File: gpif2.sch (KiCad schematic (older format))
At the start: 38 parts, among them Q3 IRLML2502, SW1 SW_IL, U1 xc7a50tftg256

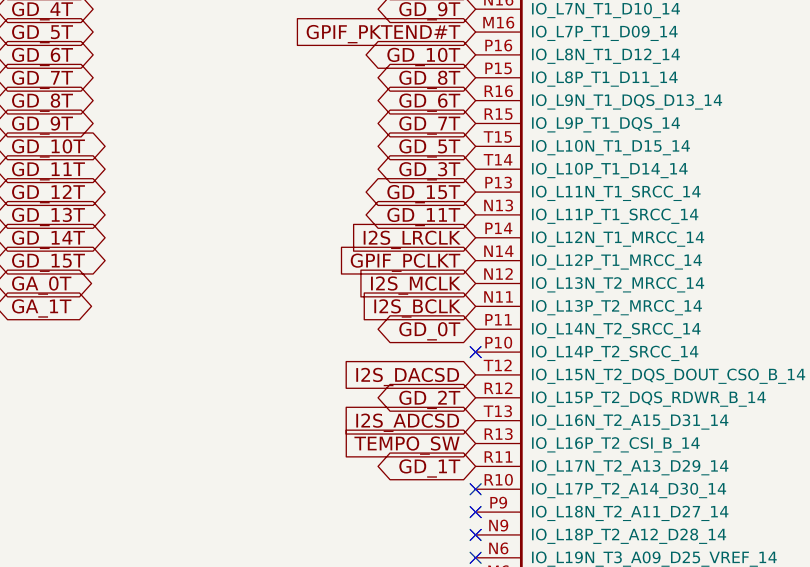
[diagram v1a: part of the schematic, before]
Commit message: finished most non-priority connections and placed power/gnd planes
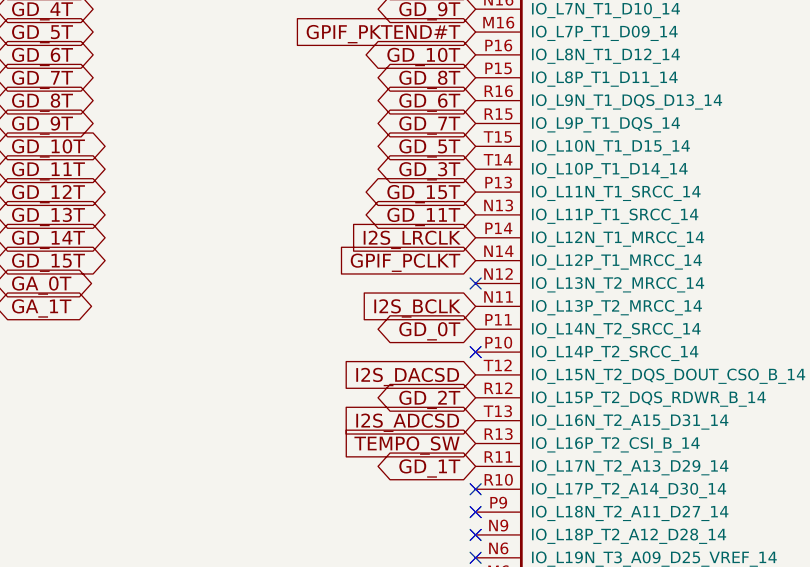
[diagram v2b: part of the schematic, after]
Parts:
- R33: footprint Resistors_SMD:R_1206 -> Resistors_SMD:R_0402
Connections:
- net I2S_MCLK: no longer names the net of U1.N12 (IO_L13N_T2_MRCC_14)
- no-connect marks 17 -> 18
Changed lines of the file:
@@
 LIBS:au-y1008-2
 LIBS:hdmi_conn
+LIBS:wayne_and_layne_kicad_symbols
 EELAYER 25 0
 EELAYER END
@@
 Text GLabel 5950 3950 0    60   Input ~ 0
 I2S_LRCLK
-Text GLabel 5950 4150 0    60   Input ~ 0
-I2S_MCLK
 Text GLabel 5950 4250 0    60   Input ~ 0
 I2S_BCLK
@@
 F 0 "R33" H 10030 3670 50  0000 L CNN
 F 1 "165" H 10030 3610 50  0000 L CNN
-F 2 "Resistors_SMD:R_1206" H 10000 3650 50  0001 C CNN
+F 2 "Resistors_SMD:R_0402" H 10000 3650 50  0001 C CNN
 F 3 "" H 10000 3650 50  0000 C CNN
 	1    10000 3650
@@
 GD_1T
 NoConn ~ 5950 1550
+NoConn ~ 5950 4150
 $EndSCHEMATC

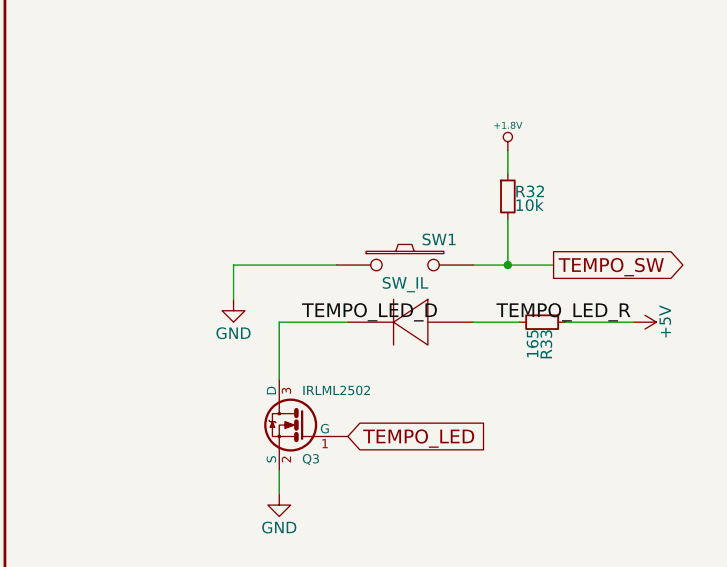
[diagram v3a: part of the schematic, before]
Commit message: changed led driver footprint, added the appropriate amount of clearence for audio jacks, redid all those connections, etc, etc
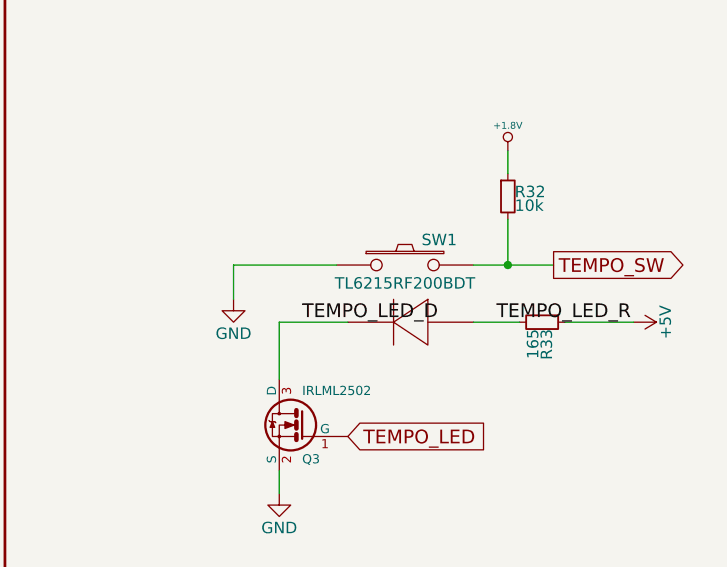
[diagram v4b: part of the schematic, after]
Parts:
- SW1: value SW_IL -> TL6215RF200BDT
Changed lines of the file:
@@
 LIBS:wayne_and_layne_kicad_symbols
 LIBS:m24m02-dr
+LIBS:fxo-hc73
 EELAYER 25 0
 EELAYER END
@@
 P 9400 3400
 F 0 "SW1" H 9550 3510 50  0000 C CNN
-F 1 "SW_IL" H 9400 3320 50  0000 C CNN
+F 1 "TL6215RF200BDT" H 9400 3320 50  0000 C CNN
 F 2 "DFTcustom:tl6215_right_angle" H 9400 3400 50  0001 C CNN
 F 3 "" H 9400 3400 50  0000 C CNN

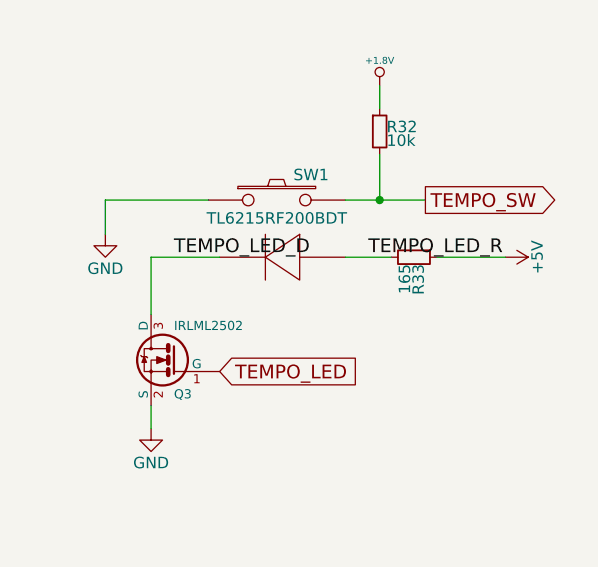
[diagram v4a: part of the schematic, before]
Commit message: completed BOM, changed footprints and values of identical components (ex. 100nf -> .1uF), have yet to update PCBNEW to reflect footprint changes
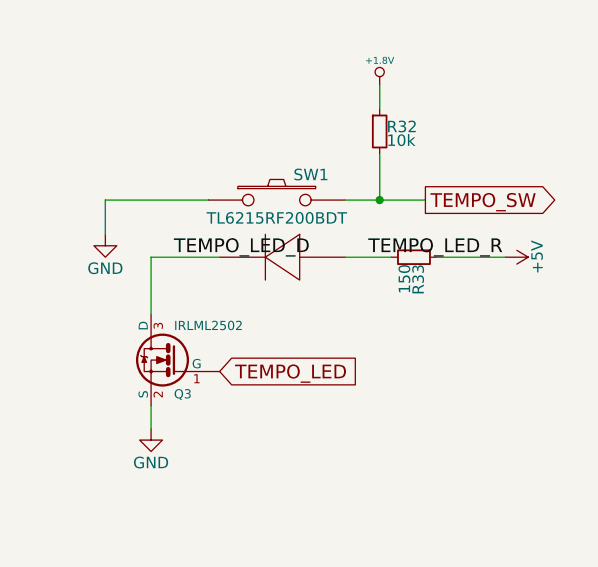
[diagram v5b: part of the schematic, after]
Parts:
- R33: value 165 -> 150
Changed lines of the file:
@@
 P 10000 3650
 F 0 "R33" H 10030 3670 50  0000 L CNN
-F 1 "165" H 10030 3610 50  0000 L CNN
+F 1 "150" H 10030 3610 50  0000 L CNN
 F 2 "Resistors_SMD:R_0402" H 10000 3650 50  0001 C CNN
 F 3 "" H 10000 3650 50  0000 C CNN

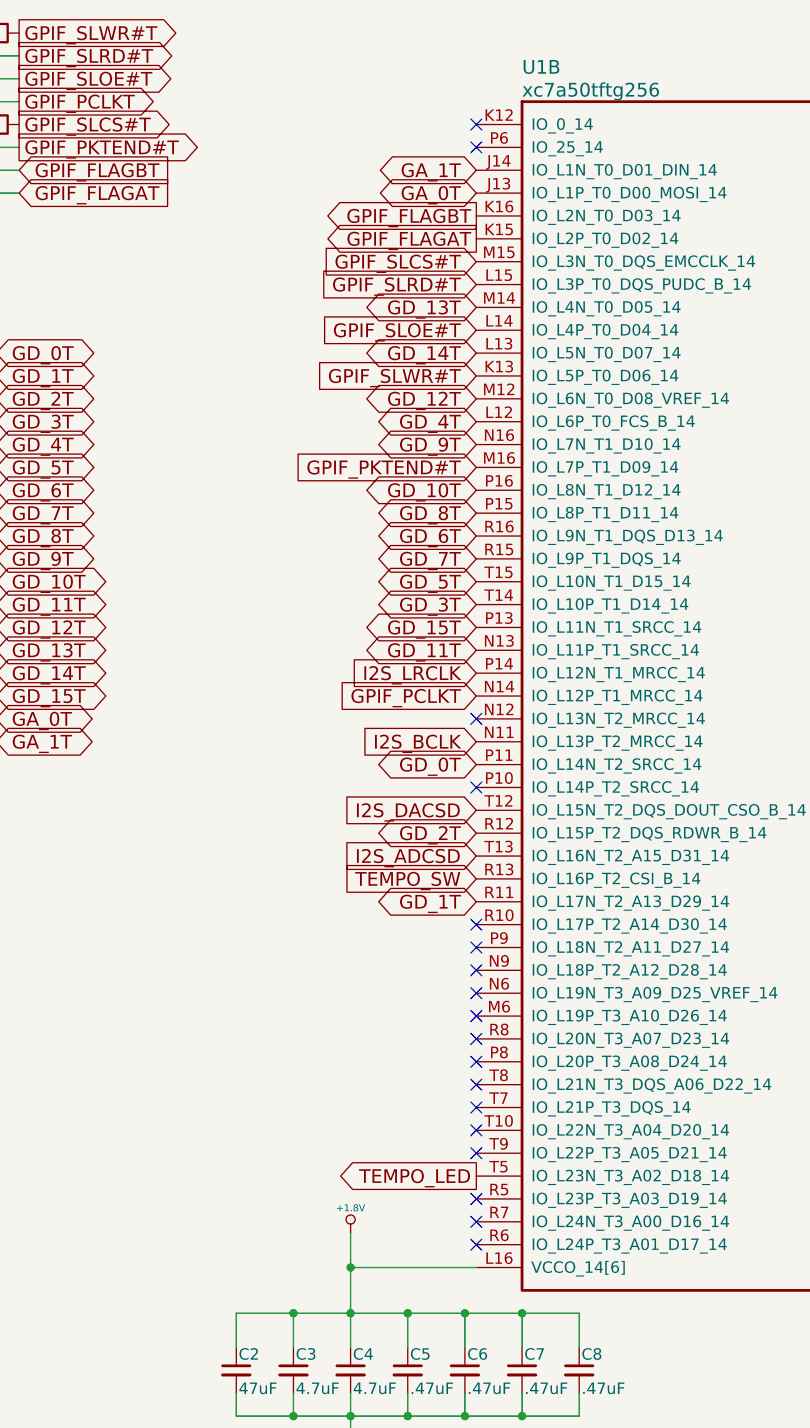
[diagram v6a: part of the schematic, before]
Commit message: added configuration data line, other small changes
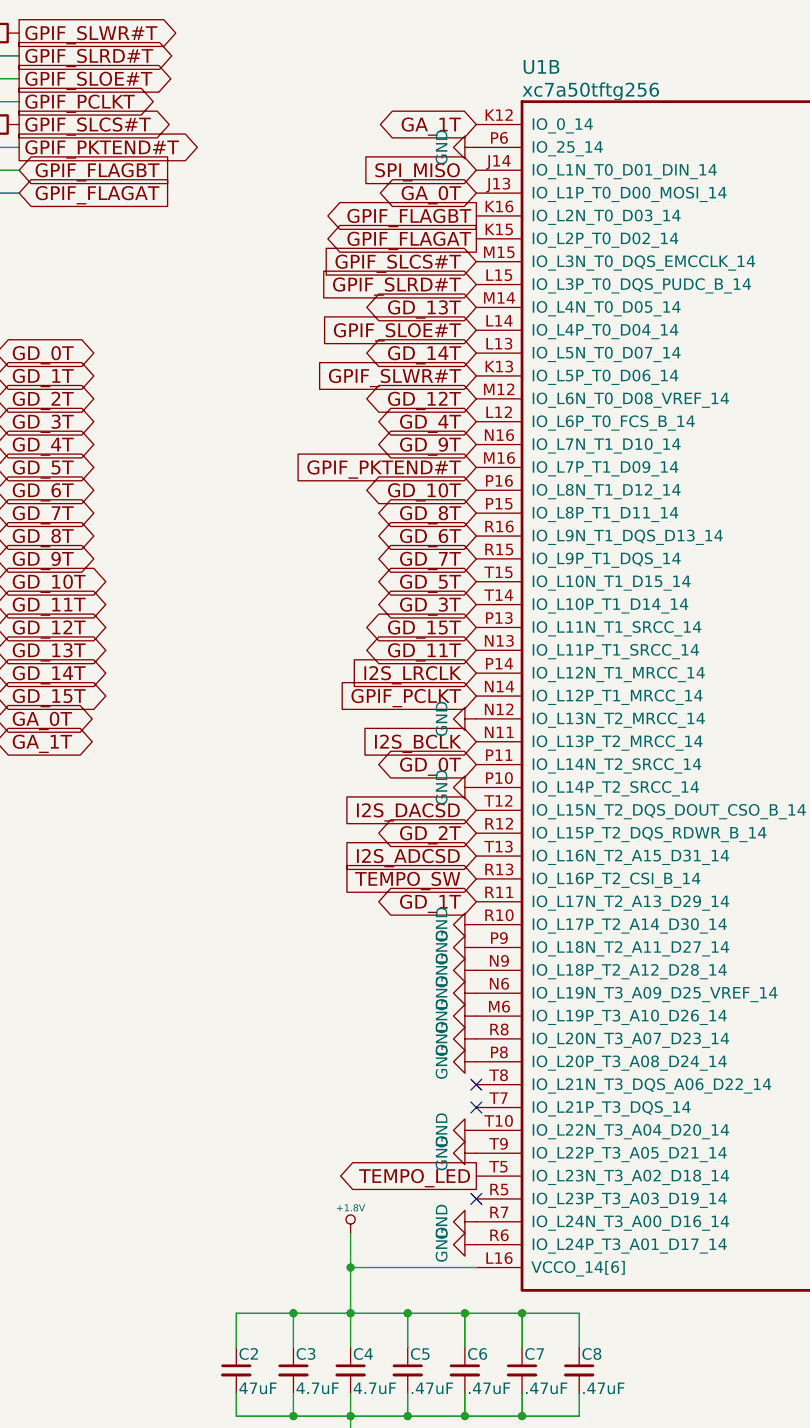
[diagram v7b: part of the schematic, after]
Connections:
- net GA_1T: now also U1.K12 (IO_0_14); no longer U1.J14 (IO_L1N_T0_D01_DIN_14)
- net GND: now also U1.M6 (IO_L19P_T3_A10_D26_14), U1.N12 (IO_L13N_T2_MRCC_14), U1.N6 (IO_L19N_T3_A09_D25_VREF_14), U1.N9 (IO_L18P_T2_A12_D28_14), U1.P10 (IO_L14P_T2_SRCC_14), U1.P6 (IO_25_14), U1.P8 (IO_L20P_T3_A08_D24_14), U1.P9 (IO_L18N_T2_A11_D27_14), U1.R10 (IO_L17P_T2_A14_D30_14), U1.R6 (IO_L24P_T3_A01_D17_14), U1.R7 (IO_L24N_T3_A00_D16_14), U1.R8 (IO_L20N_T3_A07_D23_14), U1.T10 (IO_L22N_T3_A04_D20_14), U1.T9 (IO_L22P_T3_A05_D21_14)
- new net SPI_MISO: U1.J14 (IO_L1N_T0_D01_DIN_14)
- no-connect marks 18 -> 3
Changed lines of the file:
@@
 $EndComp
 $Comp
-L +1.8V #PWR12
+L +1.8V #PWR012
 U 1 1 585C5E93
 P 5400 6400
-F 0 "#PWR12" H 5400 6540 20  0001 C CNN
+F 0 "#PWR012" H 5400 6540 20  0001 C CNN
 F 1 "+1.8V" H 5400 6510 30  0000 C CNN
 F 2 "" H 5400 6400 60  0001 C CNN
@@
 Text GLabel 2700 1450 0    60   Input ~ 0
 GPIF_PCLK
-NoConn ~ 5950 5550
 NoConn ~ 5950 6250
-NoConn ~ 5950 5050
-NoConn ~ 5950 5150
-NoConn ~ 5950 5250
-NoConn ~ 5950 5350
-NoConn ~ 5950 5450
-NoConn ~ 5950 6350
-NoConn ~ 5950 6450
 $Comp
 L C_Small C2
@@
 Connection ~ 5150 7200
 $Comp
-L GND #PWR13
+L GND #PWR013
 U 1 1 586C88E4
 P 5400 7300
-F 0 "#PWR13" H 5400 7050 50  0001 C CNN
+F 0 "#PWR013" H 5400 7050 50  0001 C CNN
 F 1 "GND" H 5400 7150 50  0000 C CNN
 F 2 "" H 5400 7300 50  0000 C CNN
@@
 Text GLabel 5950 4250 0    60   Input ~ 0
 I2S_BCLK
-NoConn ~ 5950 4450
 Text GLabel 5950 4550 0    60   Input ~ 0
 I2S_DACSD
@@
 $EndComp
 $Comp
-L GND #PWR14
+L GND #PWR014
 U 1 1 587AD7CC
 P 8650 3550
-F 0 "#PWR14" H 8650 3300 50  0001 C CNN
+F 0 "#PWR014" H 8650 3300 50  0001 C CNN
 F 1 "GND" H 8650 3400 50  0000 C CNN
 F 2 "" H 8650 3550 50  0000 C CNN
@@
 $EndComp
 $Comp
-L GND #PWR15
+L GND #PWR015
 U 1 1 587B04F2
 P 8850 4400
-F 0 "#PWR15" H 8850 4150 50  0001 C CNN
+F 0 "#PWR015" H 8850 4150 50  0001 C CNN
 F 1 "GND" H 8850 4250 50  0000 C CNN
 F 2 "" H 8850 4400 50  0000 C CNN
@@
 	9700 3650 9900 3650
 $Comp
-L +5V #PWR17
+L +5V #PWR016
 U 1 1 587B1756
 P 10400 3650
-F 0 "#PWR17" H 10400 3500 50  0001 C CNN
+F 0 "#PWR016" H 10400 3500 50  0001 C CNN
 F 1 "+5V" H 10400 3790 50  0000 C CNN
 F 2 "" H 10400 3650 50  0000 C CNN
@@
 Text GLabel 5950 4750 0    60   Input ~ 0
 I2S_ADCSD
-NoConn ~ 5950 5650
 $Comp
 L R R30
@@
 	9700 3400 10050 3400
 $Comp
-L +1.8V #PWR16
+L +1.8V #PWR017
 U 1 1 588410AE
 P 9850 2900
-F 0 "#PWR16" H 9850 3040 20  0001 C CNN
+F 0 "#PWR017" H 9850 3040 20  0001 C CNN
 F 1 "+1.8V" H 9850 3010 30  0000 C CNN
 F 2 "" H 9850 2900 60  0001 C CNN
@@
 Text Label 8950 3650 0    60   ~ 0
 TEMPO_LED_D
-NoConn ~ 5950 1650
 NoConn ~ 5950 5850
 NoConn ~ 5950 5750
-NoConn ~ 5950 5950
-NoConn ~ 5950 6050
 Text GLabel 5950 2250 0    60   Input ~ 0
 GPIF_SLRD#T
@@
 Text GLabel 5950 4050 0    60   Input ~ 0
 GPIF_PCLKT
-Text GLabel 5950 1750 0    60   BiDi ~ 0
+Text GLabel 5950 1550 0    60   BiDi ~ 0
 GA_1T
 Text GLabel 5950 1850 0    60   BiDi ~ 0
@@
 Text GLabel 5950 4950 0    60   BiDi ~ 0
 GD_1T
-NoConn ~ 5950 1550
-NoConn ~ 5950 4150
+$Comp
+L GND #PWR018
+U 1 1 58945BF9
+P 5950 4150
+F 0 "#PWR018" H 5950 3900 50  0001 C CNN
+F 1 "GND" H 5950 4000 50  0000 C CNN
+F 2 "" H 5950 4150 50  0000 C CNN
+F 3 "" H 5950 4150 50  0000 C CNN
+	1    5950 4150
+	0    1    1    0
+$EndComp
+$Comp
+L GND #PWR019
+U 1 1 589461C0
+P 5950 4450
+F 0 "#PWR019" H 5950 4200 50  0001 C CNN
+F 1 "GND" H 5950 4300 50  0000 C CNN
+F 2 "" H 5950 4450 50  0000 C CNN
+F 3 "" H 5950 4450 50  0000 C CNN
+	1    5950 4450
+	0    1    1    0
+$EndComp
+$Comp
+L GND #PWR020
+U 1 1 58946355
+P 5950 5050
+F 0 "#PWR020" H 5950 4800 50  0001 C CNN
+F 1 "GND" H 5950 4900 50  0000 C CNN
+F 2 "" H 5950 5050 50  0000 C CNN
+F 3 "" H 5950 5050 50  0000 C CNN
+	1    5950 5050
+	0    1    1    0
+$EndComp
+$Comp
+L GND #PWR021
+U 1 1 58946634
+P 5950 5950
+F 0 "#PWR021" H 5950 5700 50  0001 C CNN
+F 1 "GND" H 5950 5800 50  0000 C CNN
+F 2 "" H 5950 5950 50  0000 C CNN
+F 3 "" H 5950 5950 50  0000 C CNN
+	1    5950 5950
+	0    1    1    0
+$EndComp
+$Comp
+L GND #PWR022
+U 1 1 589483E2
+P 5950 1650
+F 0 "#PWR022" H 5950 1400 50  0001 C CNN
+F 1 "GND" H 5950 1500 50  0000 C CNN
+F 2 "" H 5950 1650 50  0000 C CNN
+F 3 "" H 5950 1650 50  0000 C CNN
+	1    5950 1650
+	0    1    1    0
+$EndComp
+$Comp
+L GND #PWR023
+U 1 1 58948C63
+P 5950 6450
+F 0 "#PWR023" H 5950 6200 50  0001 C CNN
+F 1 "GND" H 5950 6300 50  0000 C CNN
+F 2 "" H 5950 6450 50  0000 C CNN
+F 3 "" H 5950 6450 50  0000 C CNN
+	1    5950 6450
+	0    1    1    0
+$EndComp
+$Comp
+L GND #PWR024
+U 1 1 5894C026
+P 5950 6350
+F 0 "#PWR024" H 5950 6100 50  0001 C CNN
+F 1 "GND" H 5950 6200 50  0000 C CNN
+F 2 "" H 5950 6350 50  0000 C CNN
+F 3 "" H 5950 6350 50  0000 C CNN
+	1    5950 6350
+	0    1    1    0
+$EndComp
+$Comp
+L GND #PWR025
+U 1 1 5894C0A3
+P 5950 5650
+F 0 "#PWR025" H 5950 5400 50  0001 C CNN
+F 1 "GND" H 5950 5500 50  0000 C CNN
+F 2 "" H 5950 5650 50  0000 C CNN
+F 3 "" H 5950 5650 50  0000 C CNN
+	1    5950 5650
+	0    1    1    0
+$EndComp
+$Comp
+L GND #PWR026
+U 1 1 5894C120
+P 5950 5550
+F 0 "#PWR026" H 5950 5300 50  0001 C CNN
+F 1 "GND" H 5950 5400 50  0000 C CNN
+F 2 "" H 5950 5550 50  0000 C CNN
+F 3 "" H 5950 5550 50  0000 C CNN
+	1    5950 5550
+	0    1    1    0
+$EndComp
+$Comp
+L GND #PWR027
+U 1 1 5894C19D
+P 5950 5250
+F 0 "#PWR027" H 5950 5000 50  0001 C CNN
+F 1 "GND" H 5950 5100 50  0000 C CNN
+F 2 "" H 5950 5250 50  0000 C CNN
+F 3 "" H 5950 5250 50  0000 C CNN
+	1    5950 5250
+	0    1    1    0
+$EndComp
+$Comp
+L GND #PWR028
+U 1 1 5894C21A
+P 5950 5150
+F 0 "#PWR028" H 5950 4900 50  0001 C CNN
+F 1 "GND" H 5950 5000 50  0000 C CNN
+F 2 "" H 5950 5150 50  0000 C CNN
+F 3 "" H 5950 5150 50  0000 C CNN
+	1    5950 5150
+	0    1    1    0
+$EndComp
+$Comp
+L GND #PWR029
+U 1 1 5894C331
+P 5950 6050
+F 0 "#PWR029" H 5950 5800 50  0001 C CNN
+F 1 "GND" H 5950 5900 50  0000 C CNN
+F 2 "" H 5950 6050 50  0000 C CNN
+F 3 "" H 5950 6050 50  0000 C CNN
+	1    5950 6050
+	0    1    1    0
+$EndComp
+$Comp
+L GND #PWR030
+U 1 1 5894CCAA
+P 5950 5350
+F 0 "#PWR030" H 5950 5100 50  0001 C CNN
+F 1 "GND" H 5950 5200 50  0000 C CNN
+F 2 "" H 5950 5350 50  0000 C CNN
+F 3 "" H 5950 5350 50  0000 C CNN
+	1    5950 5350
+	0    1    1    0
+$EndComp
+$Comp
+L GND #PWR031
+U 1 1 5894CD27
+P 5950 5450
+F 0 "#PWR031" H 5950 5200 50  0001 C CNN
+F 1 "GND" H 5950 5300 50  0000 C CNN
+F 2 "" H 5950 5450 50  0000 C CNN
+F 3 "" H 5950 5450 50  0000 C CNN
+	1    5950 5450
+	0    1    1    0
+$EndComp
+Text GLabel 5950 1750 0    60   Input ~ 0
+SPI_MISO
 $EndSCHEMATC
